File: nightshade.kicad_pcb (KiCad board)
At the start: 4 copper layers, 154.6 x 71.8 mm, 103 parts, among them J1 Conn_02x13_Odd_Even, J2 Bus_ISA_16bit, J3 DB15_Female_HighDensity_Mount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, U1 GD542x_ISA, U2 SOJ_256Kx16, U3 SOJ_256Kx16, U4 LM334SM, U5 27C010, U6 'LS/ALS/F244, Y1 14.31818MHz

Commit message: Add files via upload
Updated to Version 0.8
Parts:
- removed C40: 0.1u, Capacitor_SMD:C_0805_2012Metric
- removed R20, R21: 6.8K, Resistor_SMD:R_0603_1608Metric
- added C51: 0.1u, Capacitor_SMD:C_0805_2012Metric, B.Cu at (104.5, 92.0)
- added C52: 0.1u, Capacitor_SMD:C_0805_2012Metric, F.Cu at (87.5, 102.8)
- added C53: 0.1u, Capacitor_SMD:C_0805_2012Metric, B.Cu at (111.1, 101.1)
- added C54: 0.1u, Capacitor_SMD:C_0805_2012Metric, F.Cu at (93.0, 125.8)
- added C55: 0.1u, Capacitor_SMD:C_0805_2012Metric, B.Cu at (106.3, 127.5)
- added C56: 0.1u, Capacitor_SMD:C_0805_2012Metric, F.Cu at (93.1, 93.2)
- added U7: SOJ_256Kx16, SOJ_DRAM:SOJ-40_10.16x26.44mm_P1.27mm, B.Cu at (122.0, 109.7)
- added U8: SOJ_256Kx16, SOJ_DRAM:SOJ-40_10.16x26.44mm_P1.27mm, B.Cu at (101.2, 109.8)
- C1, C23, C6: moved to B.Cu
- moved G1 47.1 mm to (161.8, 122.0)
- moved C6 45.0 mm to (133.2, 104.1), turned to 180 degrees
- moved C23 40.5 mm to (127.0, 128.0), turned to -90 degrees
- moved D1 38.5 mm to (178.5, 85.7), turned to 0 degrees
- moved R14 37.4 mm to (177.5, 88.4), turned to -90 degrees
- moved R15 37.1 mm to (179.5, 88.4), turned to 90 degrees
- moved C1 31.7 mm to (126.0, 92.8), turned to 0 degrees
- moved U4 27.8 mm to (184.5, 90.2), turned to 0 degrees
- moved C20 24.7 mm to (179.7, 91.9), turned to -90 degrees
- moved C21 24.4 mm to (177.7, 91.9), turned to -90 degrees
- moved C19 24.4 mm to (174.9, 92.8), turned to 0 degrees
- moved C36 16.8 mm to (199.2, 114.7)
- moved C43 16.8 mm to (199.2, 110.8)
- moved R27 16.1 mm to (201.2, 112.8), turned to 0 degrees
- moved C37 15.5 mm to (203.3, 114.7)
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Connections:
- JP1 pad 1: Net-(JP1-A) -> GND
- JP2 pad 1: Net-(JP2-A) -> GND
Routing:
- net /RAS1: track 0.00 -> 61.9 mm, vias 0 -> 3
- net /RAS0: track 41.8 -> 88.9 mm, vias 3 -> 5
- net /HSYNC: track 70.1 -> 113.4 mm, vias 3 -> 2
- net /VSYNC: track 71.4 -> 114.0 mm, vias 1 -> 2
- net /VCC: track 161.8 -> 201.8 mm, vias 25 -> 26
- net GND: track 136.8 -> 98.8 mm, vias 183 -> 142
- net /MCLK: track 79.7 -> 48.0 mm
- net /IREF: track 45.3 -> 18.7 mm, vias 3 -> 0
- net Net-(J1-Pin_12): track 25.0 -> 4.05 mm
- net /BLANK: track 42.6 -> 21.8 mm
- net /VFILTER: track 16.5 -> 35.0 mm, vias 0 -> 2
- net /MD23: track 96.1 -> 78.2 mm
- net /DCLK: track 38.6 -> 21.1 mm
- net /P3: track 54.9 -> 71.6 mm, vias 3 -> 1
- net /WE: track 42.2 -> 58.8 mm, vias 3 -> 4
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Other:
- board size 154.6 x 71.8 mm -> 154.2 x 80.9 mm
- board text added: "1MB 1MB"
- board text added: "2MB 2MB"
- board text added: "ISA Version 0.8 Designed by AB"
- board text added: "Put your utterly useless and wasteful 2nd meg above"
- board text added: "R29: Zero Waitstate Enable JP3: IRQ2/9 Enable"
- board text added: "Use 29F010 or equivalent flash ROM in PLCC"
- board text removed: "29F010 or equivalent"
- board text removed: "Designed by AB - ISA Version 0.7"
- board text removed: "R29: Zero Waitstate Enable JP1: IRQ2/9 Enable"

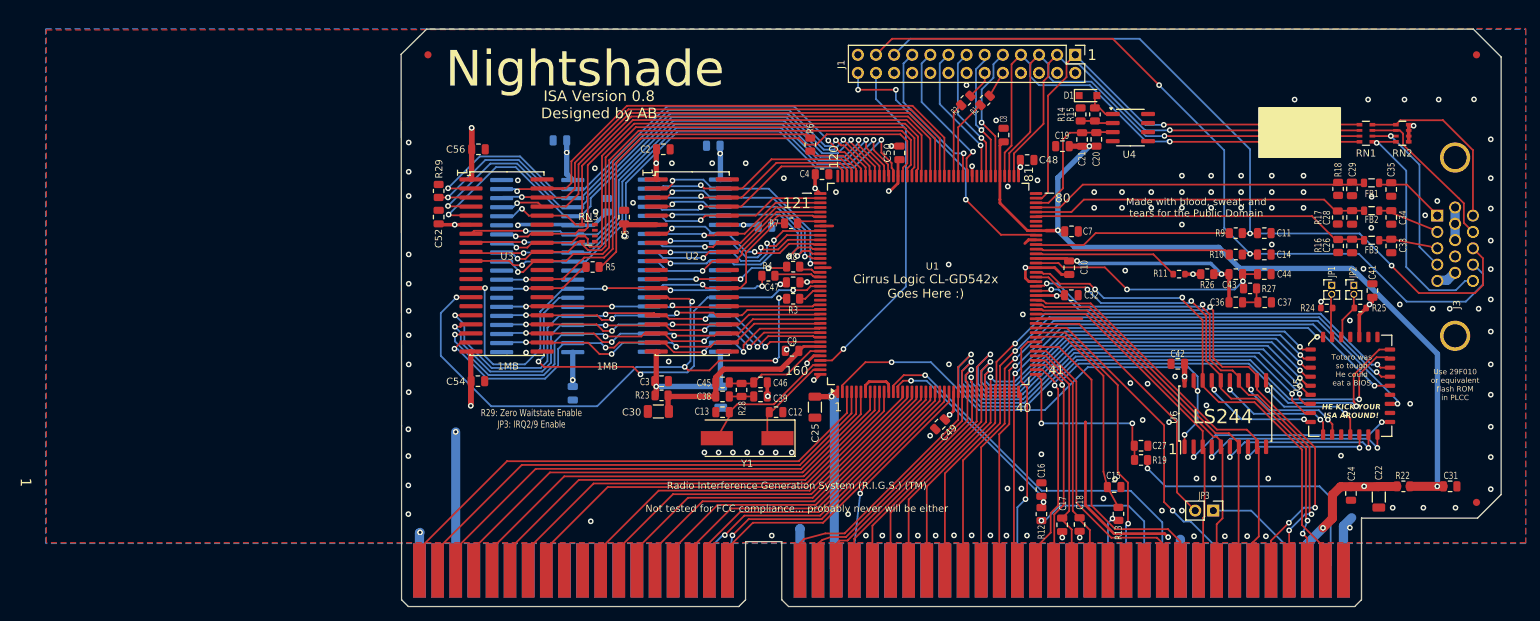
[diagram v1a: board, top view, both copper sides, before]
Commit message: Add files via upload
Uploaded version 0.8a, which fixes among other things the VFC connector pinout.
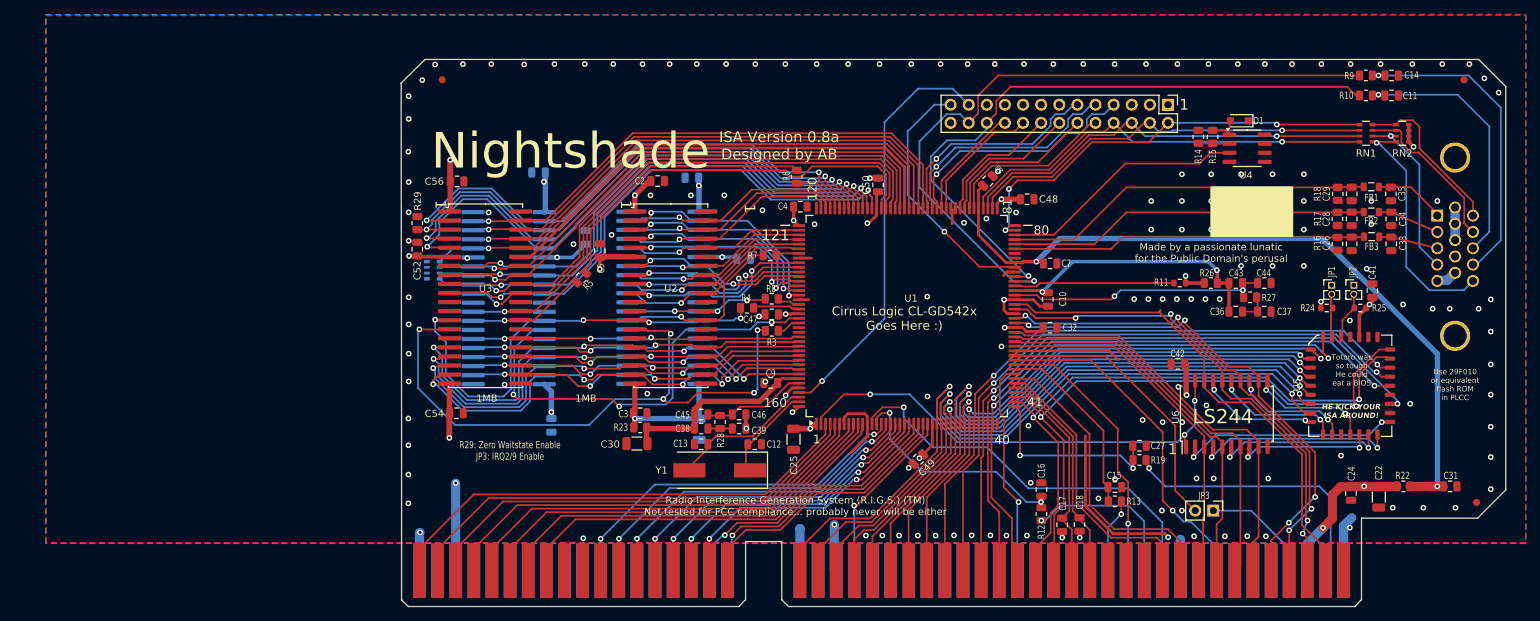
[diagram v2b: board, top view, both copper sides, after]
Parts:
- removed C19, C21: 2.2u, Capacitor_SMD:C_0805_2012Metric
- removed C20: 100p, Capacitor_SMD:C_0805_2012Metric
- removed R1, R2: 1K, Resistor_SMD:R_0805_2012Metric
- RN3: moved to B.Cu
- moved C14 30.8 mm to (221.1, 82.9)
- moved R10 28.8 mm to (217.5, 85.7), turned to 0 degrees
- moved R9 28.7 mm to (217.5, 82.9), turned to 0 degrees
- moved C11 26.3 mm to (221.1, 85.7)
- moved RN3 22.4 mm to (86.8, 110.2), turned to 0 degrees
- moved D1 21.5 mm to (199.8, 89.2), turned to 180 degrees
- moved R14 16.8 mm to (194.0, 91.5)
- moved R15 16.8 mm to (196.0, 91.5)
- moved U4 16.6 mm to (200.8, 93.1)
- moved J1 14.8 mm to (189.8, 87.0)
- moved C8 6.79 mm to (164.5, 97.7), turned to -135 degrees
- moved U8 6.02 mm to (97.2, 114.2)
- moved Y1 5.92 mm to (126.9, 138.2)
- moved C5 5.80 mm to (110.1, 107.5)
- moved C49 5.76 mm to (154.8, 136.7)
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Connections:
- C11 pad 1: /HSYNC -> Net-(C11-Pad1)
- C14 pad 1: /VSYNC -> Net-(C14-Pad1)
- J1 pad 1: /P0 -> unconnected-(J1-Pin_1-Pad1)
- J1 pad 10: Net-(J1-Pin_10) -> /P4
- J1 pad 11: /P5 -> /EDCLK
- J1 pad 12: Net-(J1-Pin_12) -> /P5
- J1 pad 13: /P6 -> /VCC
- J1 pad 14: /VCC -> /P6
- J1 pad 15: /P7 -> GND
- J1 pad 16: GND -> /P7
- J1 pad 17: /DCLK -> GND
- J1 pad 18: GND -> /DCLK
- J1 pad 19: /BLANK -> GND
- J1 pad 2: GND -> /P0
- J1 pad 20: GND -> /BLANK
- J1 pad 21: /HSYNC -> GND
- J1 pad 22: GND -> /HSYNC
- J1 pad 23: /VSYNC -> /MCLK
- J1 pad 24: /MCLK -> /VSYNC
- J1 pad 25: GND -> /OVRW
- J1 pad 26: /OVRW -> GND
- J1 pad 3: /P1 -> unconnected-(J1-Pin_3-Pad3)
- J1 pad 4: GND -> /P1
- J1 pad 5: /P2 -> unconnected-(J1-Pin_5-Pad5)
- J1 pad 6: GND -> /P2
- J1 pad 7: /P3 -> /EVIDEO
- J1 pad 8: GND -> /P3
- J1 pad 9: /P4 -> /ESYNC
- J3 pad 13: /HSYNC -> Net-(C11-Pad1)
- J3 pad 14: /VSYNC -> Net-(C14-Pad1)
- R10 pad 1: /VSYNC -> /HSYNC
- R10 pad 2: Net-(U1-VSYNC) -> Net-(C11-Pad1)
- R9 pad 1: /HSYNC -> /VSYNC
- R9 pad 2: Net-(U1-HSYNC) -> Net-(C14-Pad1)
- U1 pad 68: Net-(U1-VSYNC) -> /VSYNC
- U1 pad 69: Net-(U1-HSYNC) -> /HSYNC
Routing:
- net GND: track 98.8 -> 174.8 mm, vias 142 -> 161
- net Net-(C14-Pad1): track 0.00 -> 44.2 mm, vias 0 -> 1
- net Net-(C11-Pad1): track 0.00 -> 37.2 mm, vias 0 -> 1
- net /EDCLK: track 0.00 -> 30.5 mm, vias 0 -> 1
- net Net-(U1-HSYNC): track 27.7 -> 0.00 mm
- net Net-(U1-VSYNC): track 27.4 -> 0.00 mm
- net /VCC: track 201.8 -> 177.5 mm, vias 26 -> 27
- net /EVIDEO: track 11.2 -> 34.6 mm, vias 0 -> 1
- net /HSYNC: track 113.4 -> 90.7 mm, vias 2 -> 1
- net /ESYNC: track 10.4 -> 32.2 mm, vias 0 -> 1
- net /IREF: track 18.7 -> 34.9 mm
- net /AVcc: track 120.5 -> 105.3 mm, vias 3 -> 2
- net /VSYNC: track 114.0 -> 98.8 mm, vias 2 -> 1
- net /P3: track 71.6 -> 59.7 mm
- net /P2: track 69.4 -> 58.7 mm
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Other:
- board size 154.2 x 80.9 mm -> 154.9 x 76.7 mm
- board text added: "ISA Version 0.8a Designed by AB"
- board text added: "Made by a passionate lunatic for the Public Domain's perusal"
- board text removed: "ISA Version 0.8 Designed by AB"
- board text removed: "Made with blood, sweat, and tears for the Public Domain"

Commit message: Add files via upload
quick fixes
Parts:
- moved C55 1.05 mm to (102.2, 131.9)
- moved C52 0.56 mm to (85.0, 107.5)
- moved R29 0.50 mm to (85.0, 103.6)
- moved U3 0.42 mm to (94.5, 114.2)
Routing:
- net /MD26: track 74.3 -> 76.6 mm
- net /MA3: track 59.2 -> 60.7 mm
- net /MD25: track 79.1 -> 80.5 mm
- net /MD18: track 77.6 -> 76.3 mm
- net /RAS0: track 88.9 -> 87.6 mm
- net /MD27: track 76.6 -> 77.7 mm
- net /MD19: track 77.1 -> 76.1 mm
- net /MD17: track 77.4 -> 76.5 mm
- net /MD16: track 74.2 -> 73.4 mm
- net /MD29: track 74.9 -> 75.7 mm
- net GND: track 174.8 -> 175.5 mm
- net /MD28: track 79.8 -> 80.5 mm
- net /MA0: track 65.5 -> 64.9 mm

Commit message: Add files via upload
0.8a is finalized! Merry Christmas!
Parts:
- moved R10 8.01 mm to (210.0, 88.5)
- moved R9 7.86 mm to (210.0, 85.2)
- moved C11 7.62 mm to (214.0, 88.5)
- moved C14 7.48 mm to (214.0, 85.2)
- moved FID1 3.82 mm to (232.0, 87.2)
- moved FID3 3.82 mm to (87.2, 87.2)
- moved RN1 2.25 mm to (217.5, 93.2)
- moved RN2 2.25 mm to (222.6, 93.2)
- moved R5 2.08 mm to (105.7, 110.2), turned to -90 degrees
- moved R18 1.98 mm to (212.2, 101.0)
- moved C26 1.95 mm to (214.2, 108.0)
- moved C28 1.95 mm to (214.2, 104.5)
- moved C29 1.95 mm to (214.2, 101.0)
- moved R16 1.95 mm to (212.2, 108.0)
- moved R17 1.95 mm to (212.2, 104.5)
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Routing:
- net GND: track 175.5 -> 185.4 mm, vias 161 -> 165
- net /VSYNC: track 98.8 -> 90.8 mm
- net /MID1: track 23.0 -> 30.9 mm
- net /HSYNC: track 90.7 -> 83.0 mm
- net Net-(C14-Pad1): track 44.2 -> 50.3 mm
- net Net-(C11-Pad1): track 37.2 -> 42.9 mm
- net /MID0: track 22.8 -> 28.0 mm
- net /VCC: track 177.2 -> 172.3 mm
- net /MID3: track 33.9 -> 31.3 mm
- net /MA2: track 59.1 -> 61.4 mm
- net /RED: track 51.9 -> 49.8 mm
- net /MA1: track 61.3 -> 63.4 mm
- net /GREEN: track 50.8 -> 48.9 mm
- net /~{MEMR}: track 32.4 -> 34.1 mm
- net /EDCLK: track 30.5 -> 32.1 mm
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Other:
- board size 154.9 x 76.7 mm -> 154.9 x 75.5 mm
- board text added: "But what _is_ this actually good for? Hmmm..."
- board text added: "Give me a 29F010, bartender!"
- board text added: "IRQ2/9 Enable"
- board text added: "Now I'm got a craving for... canned ravioli?"
- board text added: "R29: Zero Waitstate Enable"
- board text added: "This is *NOT* a floppy connector"
- board text removed: "HE KICK YOUR ISA AROUND!"
- board text removed: "It ain't easy (It ain't easy) But now I know I like it that way"
- board text removed: "R29: Zero Waitstate Enable JP3: IRQ2/9 Enable"
- board text removed: "Totoro was so tough He could eat a BIOS"
- board text removed: "Use 29F010 or equivalent flash ROM in PLCC"

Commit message: Add files via upload
Updated to version 0.8b. Merry Christmas!
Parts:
- removed C36, C38: 2.2u, Capacitor_SMD:C_0805_2012Metric
- removed C43, C45: 0.22u, Capacitor_SMD:C_0805_2012Metric
- removed C9: 0.1u, Capacitor_SMD:C_0805_2012Metric
- removed R23, R26: 33, Resistor_SMD:R_0805_2012Metric
- added FB4: 0805-HiZ, No Resonance, Inductor_SMD:L_0805_2012Metric, F.Cu at (175.7, 113.2)
- added FB5: 0805-HiZ, No Resonance, Inductor_SMD:L_0805_2012Metric, F.Cu at (116.0, 132.5)
- C12, C13: value 22p -> C_Small
- Y1: footprint Crystal:Crystal_SMD_HC49-SD -> Crystal:Crystal_SMD_5032-2Pin_5.0x3.2mm_HandSoldering
- moved C44 23.7 mm to (179.8, 115.2), turned to -90 degrees
- moved R27 18.8 mm to (182.5, 114.5)
- moved C37 18.0 mm to (185.2, 115.2), turned to 90 degrees
- moved R11 15.5 mm to (175.9, 111.5)
- moved C22 5.04 mm to (214.3, 142.4), turned to 0 degrees
- moved C30 4.98 mm to (120.2, 134.0), turned to -90 degrees
- moved C13 4.68 mm to (128.7, 136.2), turned to 180 degrees
- moved C39 4.62 mm to (125.2, 131.2), turned to 90 degrees
- moved Y1 4.22 mm to (129.3, 139.4)
- moved C24 3.49 mm to (213.8, 144.6), turned to 0 degrees
- moved C52 1.95 mm to (85.5, 109.5), turned to 90 degrees
- moved R29 1.82 mm to (85.5, 105.4), turned to 90 degrees
- moved C12 1.65 mm to (132.2, 136.2), turned to 0 degrees
- moved R28 1.40 mm to (127.8, 130.4), turned to 180 degrees
- moved C46 1.17 mm to (130.5, 131.2), turned to -90 degrees
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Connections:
- C12 pad 1: GND -> /OSC
- C12 pad 2: Net-(U1-OSC) -> GND
- C13 pad 1: GND -> /XTAL
- C13 pad 2: Net-(U1-XTAL) -> GND
- C37 pad 1: Net-(C36-Pad2) -> GND
- C37 pad 2: GND -> Net-(C37-Pad2)
- C39 pad 1: Net-(C38-Pad2) -> GND
- C39 pad 2: GND -> Net-(C39-Pad2)
- C42 pad 1: GND -> /VCC
- C42 pad 2: /VCC -> GND
- R27 pad 2: Net-(C36-Pad2) -> Net-(C37-Pad2)
- R28 pad 2: Net-(C38-Pad2) -> Net-(C39-Pad2)
- U1 pad 158: Net-(U1-XTAL) -> /XTAL
- U1 pad 159: Net-(U1-OSC) -> /OSC
- Y1 pad 1: Net-(U1-OSC) -> /OSC
- Y1 pad 2: Net-(U1-XTAL) -> /XTAL
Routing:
- net /VCLKVCC: track 41.0 -> 6.93 mm, vias 2 -> 0
- net /VFILTER: track 36.8 -> 13.7 mm, vias 2 -> 0
- net Net-(U1-XTAL): track 19.1 -> 0.00 mm
- net /XTAL: track 0.00 -> 17.3 mm
- net /TWR: track 22.6 -> 7.27 mm
- net /OSC: track 0.00 -> 14.4 mm
- net Net-(U1-OSC): track 12.4 -> 0.00 mm
- net GND: track 185.4 -> 179.7 mm, vias 165 -> 156
- net /VCC: track 172.3 -> 168.0 mm, vias 27 -> 26
- net Net-(C36-Pad2): track 3.96 -> 0.00 mm
- net /MFILTER: track 14.6 -> 11.0 mm
- net Net-(C38-Pad2): track 3.42 -> 0.00 mm
- net /MCLKVCC: track 26.9 -> 23.9 mm
- net Net-(C37-Pad2): track 0.00 -> 1.92 mm
- net Net-(C39-Pad2): track 0.00 -> 1.82 mm
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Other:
- board text added: "ISA Version 0.8b Designed by AB"
- board text removed: "ISA Version 0.8a Designed by AB"
